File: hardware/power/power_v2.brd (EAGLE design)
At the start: 92 x 92 mm, 57 parts, among them J1 FASTON1289_ST, J2 FASTON1289_ST, J3 12v, J4 5v, J5 XT30PW-F, J6 XT30PW-F, J7 XT30PW-F, J8 XT30PW-F, Q1 MMBT5401L, Q2 PSMN1R0-40YSH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

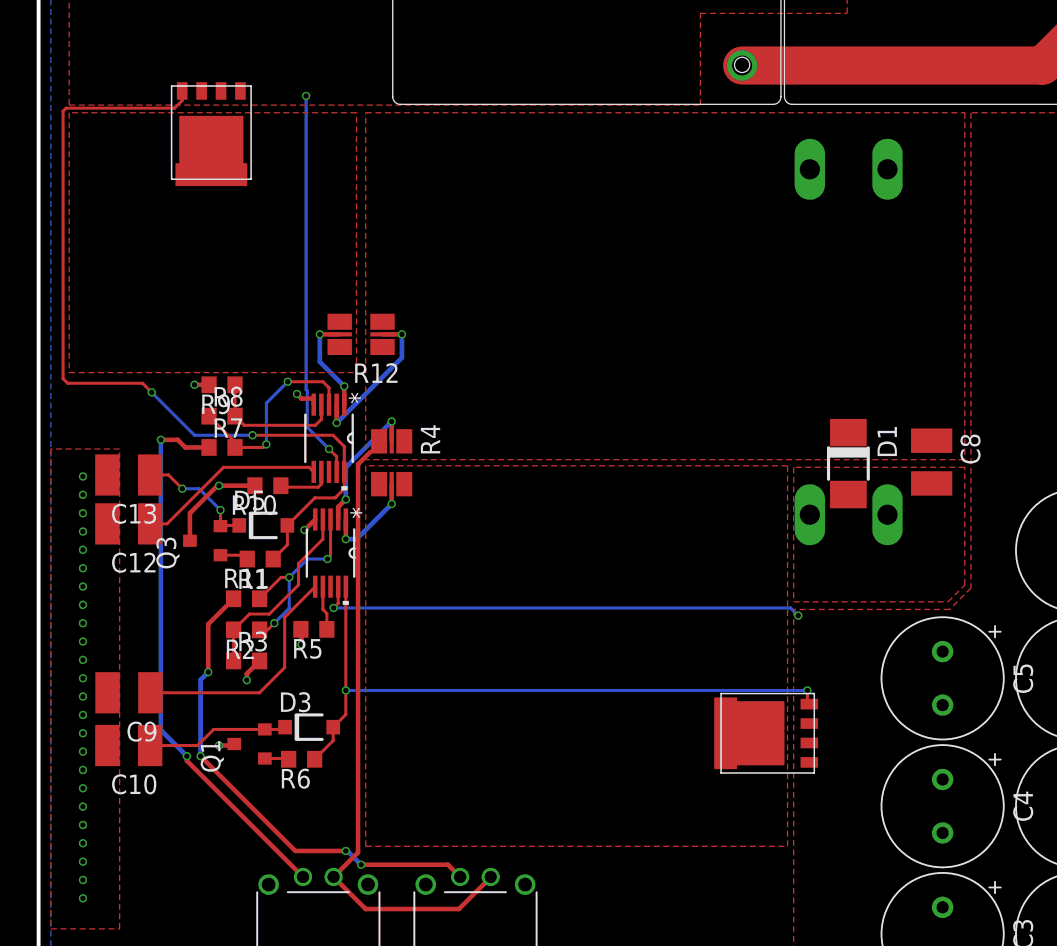
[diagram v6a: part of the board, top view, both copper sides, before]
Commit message: Added more accurate current limit resistors
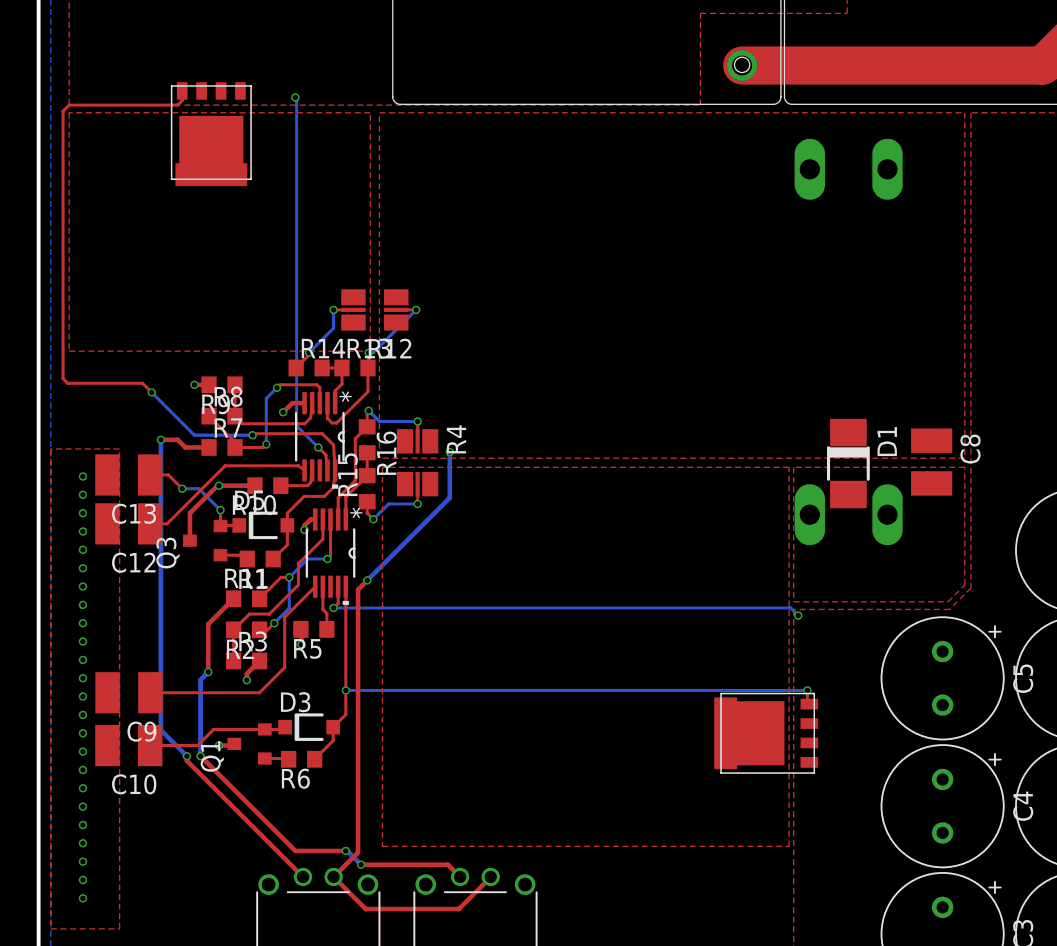
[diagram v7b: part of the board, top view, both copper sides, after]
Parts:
- added R13, R16: 10, rcl:R0603
- added R14, R15: 4.53, rcl:R0603
- moved R12 1.84 mm to (22.0, 48.1)
- moved R4 1.70 mm to (24.8, 38.1)
- moved U$14 0.61 mm to (18.4, 39.8)
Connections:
- new net N$21: R12.2_KELVIN, R14.1
- new net N$22: R12.1_KELVIN, R13.2, U$14.2
- net N$10: now also R15.2, R16.2, U$1.1; no longer R4.1_KELVIN, U$1.2
- net N$11: now also R15.1; no longer U$1.1
- net N$19: now also R16.1, R4.1_KELVIN, U$1.2; no longer R12.1_KELVIN, U$14.2
- net N$20: now also R13.1, R14.2; no longer R12.2_KELVIN
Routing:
- net N$22: track 0.00 -> 12.8 mm, vias 0 -> 2
- net N$21: track 0.00 -> 6.11 mm, vias 0 -> 2
- net N$10: track 9.16 -> 4.94 mm, vias 2 -> 0
- net N$20: track 6.56 -> 3.79 mm, vias 2 -> 0
- net N$19: track 10.0 -> 12.7 mm
- net +24V_BATT: track 40.8 -> 43.0 mm, vias 0 -> 2
- net N$14: track 56.5 -> 55.7 mm
- net N$12: track 9.07 -> 8.34 mm
- net N$15: track 3.57 -> 2.84 mm
- net N$4: track 13.5 -> 12.8 mm
- net N$11: track 6.54 -> 5.93 mm
- net N$16: track 12.4 -> 11.8 mm

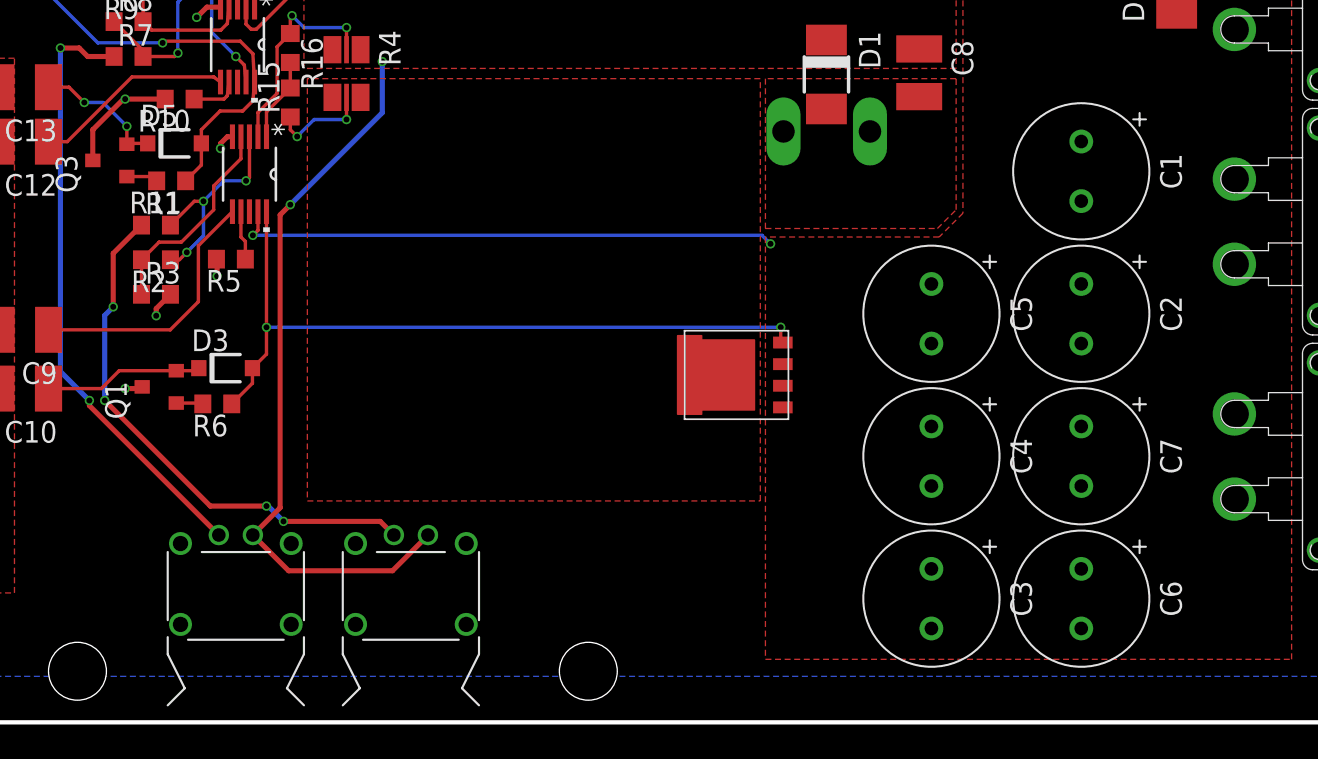
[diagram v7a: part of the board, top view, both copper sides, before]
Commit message: Moved caps a bit and redid switch wiring
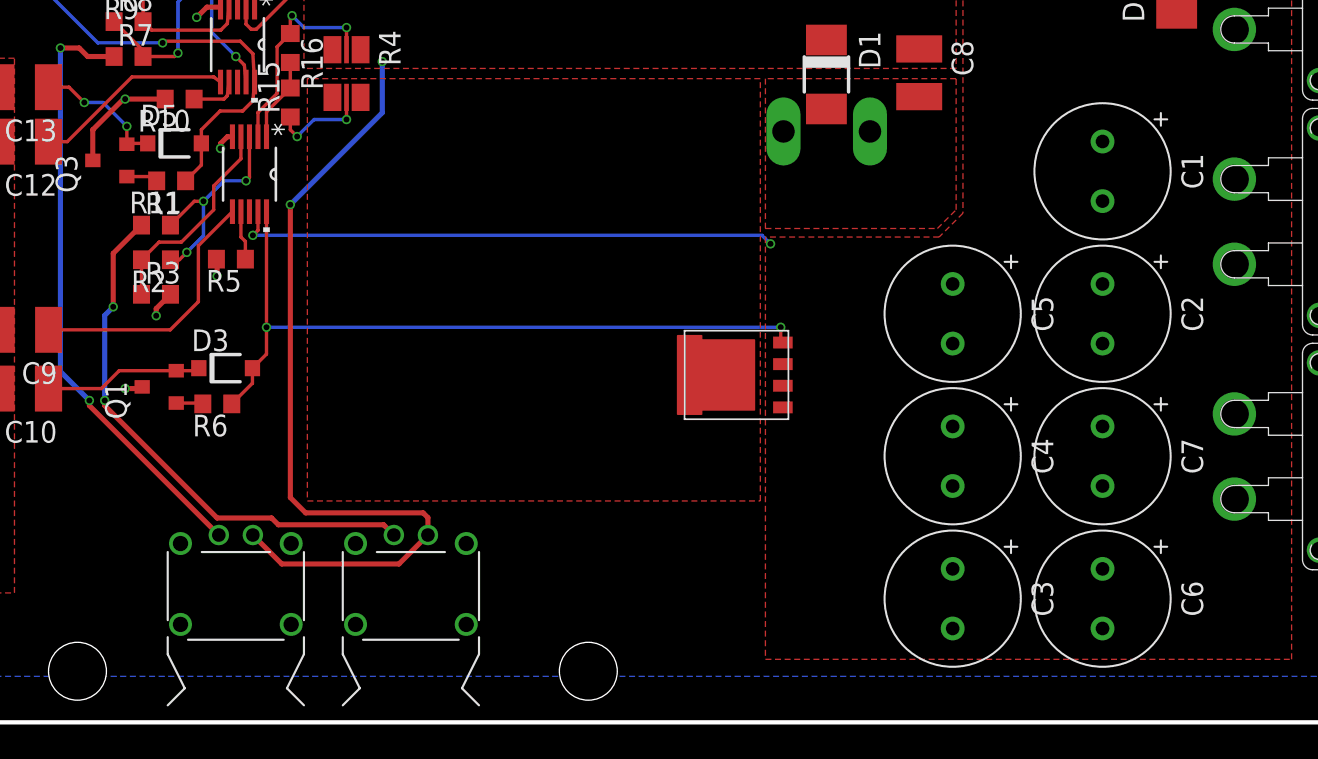
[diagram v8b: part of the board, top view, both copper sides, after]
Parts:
- moved C1 1.25 mm to (69.2, 32.4)
- moved C2 1.25 mm to (69.2, 24.0)
- moved C3 1.25 mm to (60.4, 7.26)
- moved C4 1.25 mm to (60.4, 15.6)
- moved C5 1.25 mm to (60.4, 24.0)
- moved C6 1.25 mm to (69.2, 7.26)
- moved C7 1.25 mm to (69.2, 15.6)
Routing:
- net +24V_BATT: track 43.0 -> 49.1 mm
- net N$3: track 31.4 -> 31.6 mm, vias 4 -> 2
